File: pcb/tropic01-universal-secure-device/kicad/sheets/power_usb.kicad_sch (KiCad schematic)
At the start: 0 parts

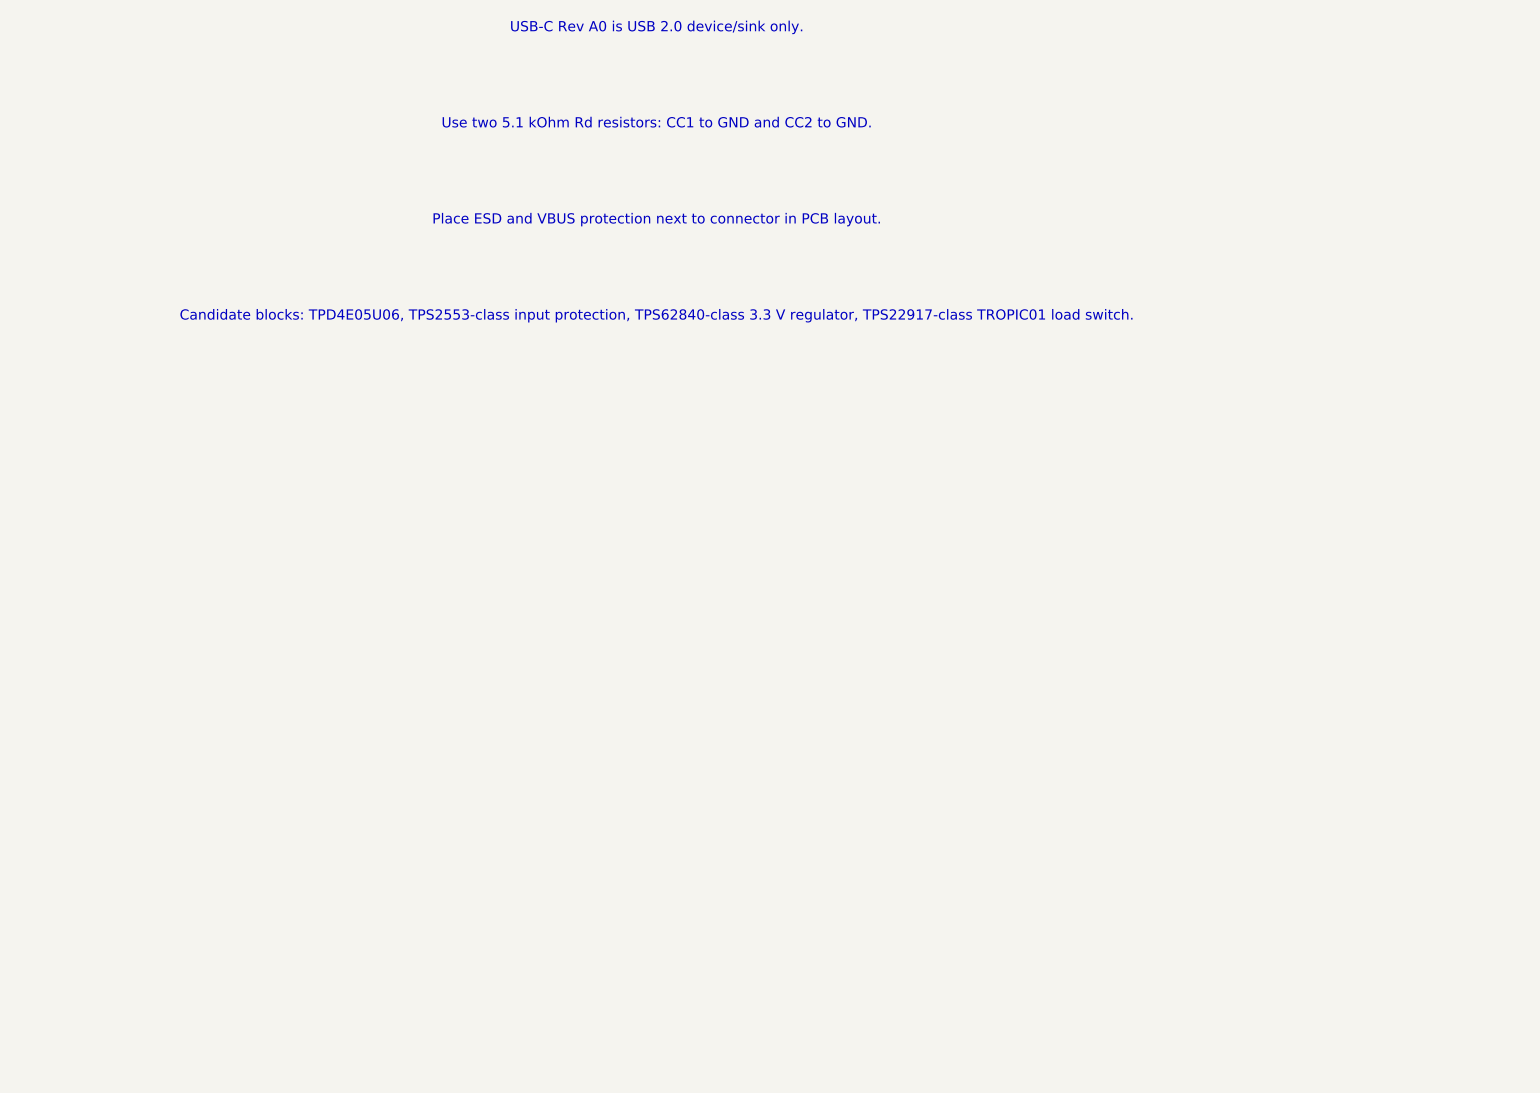
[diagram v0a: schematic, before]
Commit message: feat: materialize tropic01 schematic bindings
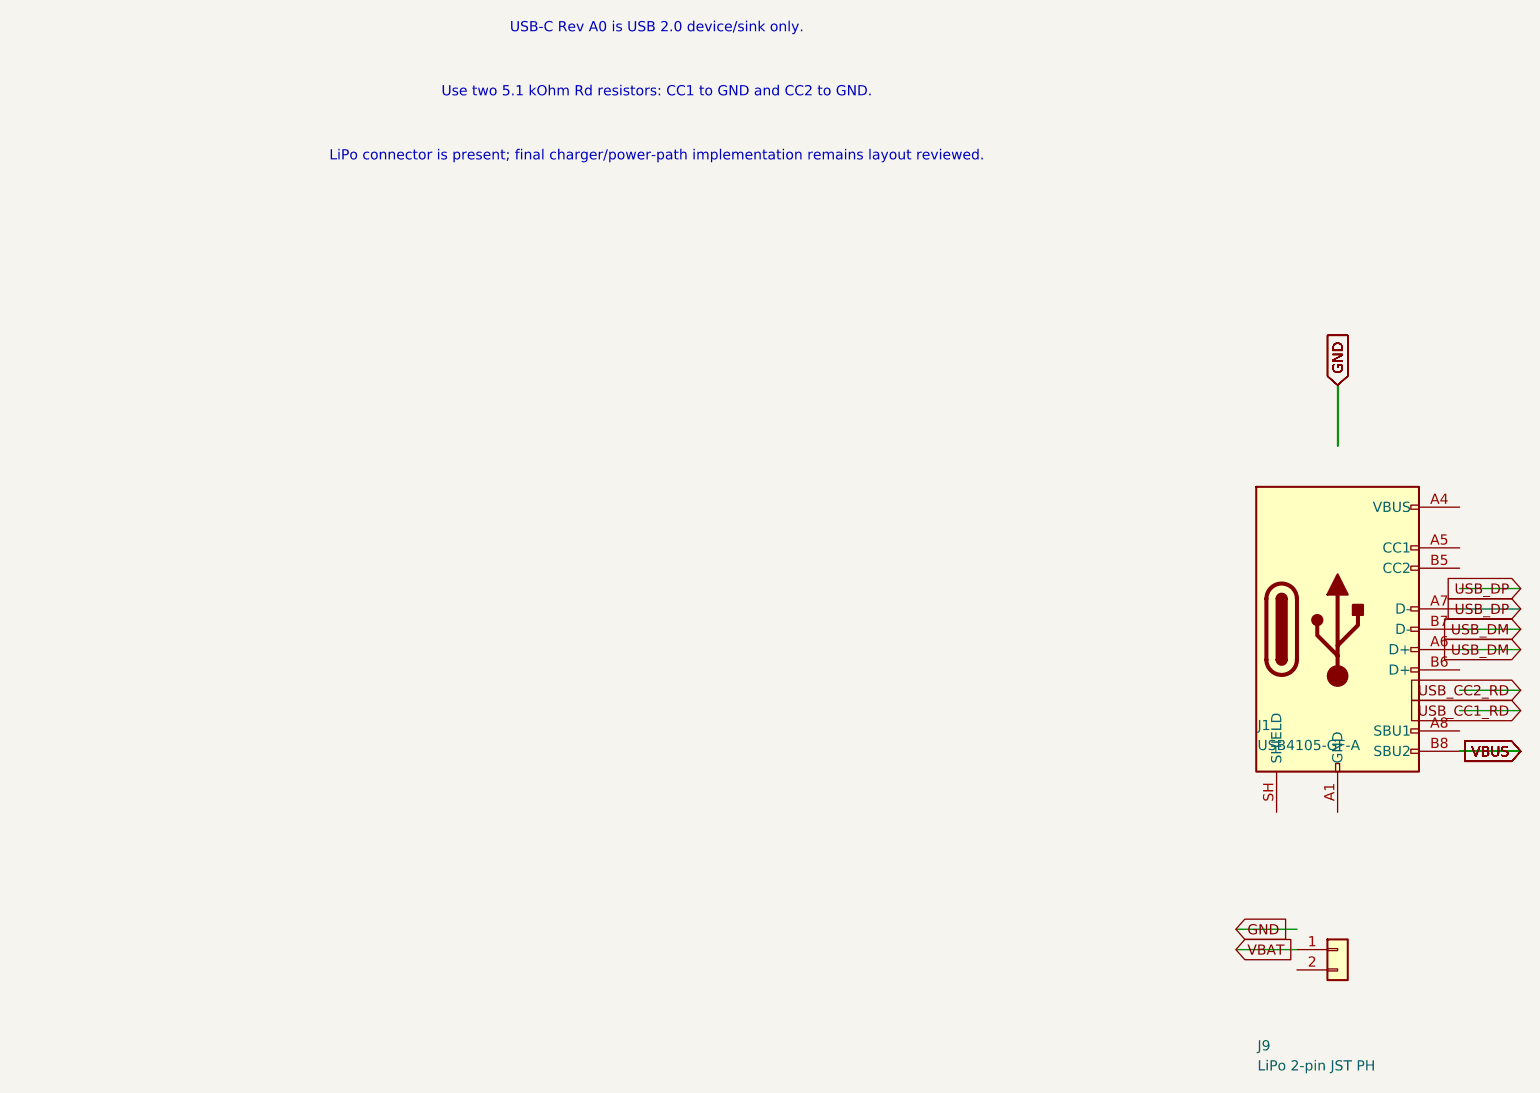
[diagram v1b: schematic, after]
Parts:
- added J1: USB4105-GF-A, Connector_USB:USB_C_Receptacle_GCT_USB4105-xx-A_16P_TopMnt_Horizontal, symbol Connector:USB_C_Receptacle_USB2.0_16P
- added J9: LiPo 2-pin JST PH, Connector_JST:JST_PH_S2B-PH-SM4-TB_1x02-1MP_P2.00mm_Horizontal, symbol Connector_Generic:Conn_01x02
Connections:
- new net: J1.A1 (GND), J1.A12 (GND), J1.B1 (GND), J1.B12 (GND)
- new net: J1.A4 (VBUS), J1.A9 (VBUS), J1.B4 (VBUS), J1.B9 (VBUS)
- new net USB_DM: J1.A6 (D+), J1.B7 (D-)
- new net USB_DP: J1.A7 (D-)
- new net VBAT: J9.1 (Pin_1)
- new net VBUS: J1.B8 (SBU2)
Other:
- note added: "LiPo connector is present; final charger/power-path implementation remains layout reviewed."
- note removed: "Candidate blocks: TPD4E05U06, TPS2553-class input protection, TPS62840-class 3.3 V regulator, TPS22917-class TROPIC01 load switch."
- note removed: "Place ESD and VBUS protection next to connector in PCB layout."

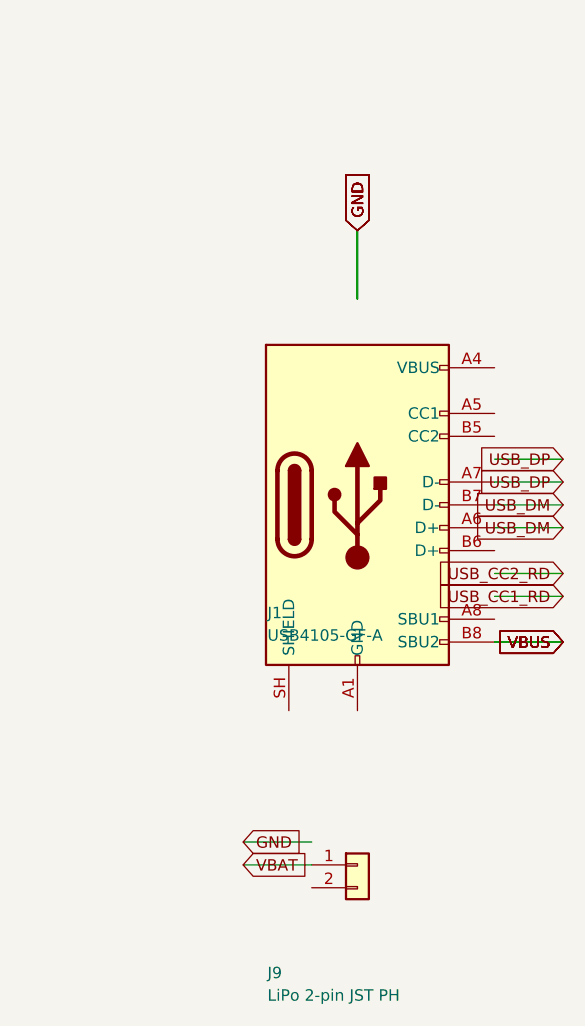
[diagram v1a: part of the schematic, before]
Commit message: feat: bind tropic01 pcb nets
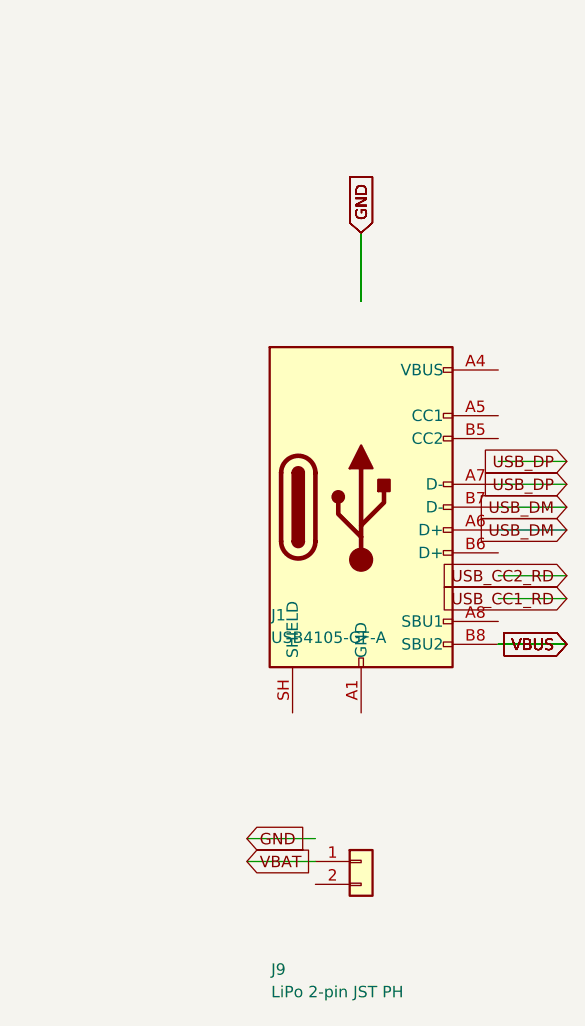
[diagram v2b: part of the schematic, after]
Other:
- moved on the sheet: J9
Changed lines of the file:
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@@
 	(symbol
 		(lib_id "Connector:USB_C_Receptacle_USB2.0_16P")
-		(at 105.00 95.00 0)
+		(at 105.41 95.25 0)
 		(unit 1)
 		(exclude_from_sim no)
@@
 		(dnp no)
 		(property "Reference" "J1"
-			(at 95.00 107.00 0)
+			(at 95.41 107.25 0)
 			(effects (font (size 1.27 1.27)) (justify left))
 		)
 		(property "Value" "USB4105-GF-A"
-			(at 95.00 109.50 0)
+			(at 95.41 109.75 0)
 			(effects (font (size 1.27 1.27)) (justify left))
 		)
 		(property "Footprint" "Connector_USB:USB_C_Receptacle_GCT_USB4105-xx-A_16P_TopMnt_Horizontal"
-			(at 105.00 95.00 0)
+			(at 105.41 95.25 0)
 			(effects (font (size 1.27 1.27)) (hide yes))
 		)
 		(property "Datasheet" "https://gct.co/connector/usb4105"
-			(at 105.00 95.00 0)
+			(at 105.41 95.25 0)
 			(effects (font (size 1.27 1.27)) (hide yes))
 		)
 		(property "Description" "GCT USB4105 USB 2.0 Type-C receptacle, female USB-C only"
-			(at 105.00 95.00 0)
+			(at 105.41 95.25 0)
 			(effects (font (size 1.27 1.27)) (hide yes))
 		)
@@
 	(symbol
 		(lib_id "Connector_Generic:Conn_01x02")
-		(at 105.00 135.00 0)
+		(at 105.41 134.62 0)
 		(unit 1)
 		(exclude_from_sim no)
@@
 		(dnp no)
 		(property "Reference" "J9"
-			(at 95.00 147.00 0)
+			(at 95.41 146.62 0)
 			(effects (font (size 1.27 1.27)) (justify left))
 		)
 		(property "Value" "LiPo 2-pin JST PH"
-			(at 95.00 149.50 0)
+			(at 95.41 149.12 0)
 			(effects (font (size 1.27 1.27)) (justify left))
 		)
 		(property "Footprint" "Connector_JST:JST_PH_S2B-PH-SM4-TB_1x02-1MP_P2.00mm_Horizontal"
-			(at 105.00 135.00 0)
+			(at 105.41 134.62 0)
 			(effects (font (size 1.27 1.27)) (hide yes))
 		)
 		(property "Datasheet" "https://www.jst.com/products/crimp-style-connectors-wire-to-board-type/ph-connector/"
-			(at 105.00 135.00 0)
+			(at 105.41 134.62 0)
 			(effects (font (size 1.27 1.27)) (hide yes))
 		)
 		(property "Description" "2-pin LiPo battery connector into charger/power path"
-			(at 105.00 135.00 0)
+			(at 105.41 134.62 0)
 			(effects (font (size 1.27 1.27)) (hide yes))
 		)
@@
 	(wire
 		(pts
-			(xy 105.00 72.14) (xy 105.00 64.52)
-		)
-		(stroke (width 0) (type default))
-	)
-	(global_label "GND"
-		(shape input)
-		(at 105.00 64.52 90)
-		(fields_autoplaced)
-		(effects (font (size 1.27 1.27)))
-	)
-	(wire
-		(pts
-			(xy 105.00 72.14) (xy 105.00 64.52)
-		)
-		(stroke (width 0) (type default))
-	)
-	(global_label "GND"
-		(shape input)
-		(at 105.00 64.52 90)
-		(fields_autoplaced)
-		(effects (font (size 1.27 1.27)))
-	)
-	(wire
-		(pts
-			(xy 120.24 110.24) (xy 127.86 110.24)
-		)
-		(stroke (width 0) (type default))
-	)
-	(global_label "VBUS"
-		(shape input)
-		(at 127.86 110.24 180)
-		(fields_autoplaced)
-		(effects (font (size 1.27 1.27)))
-	)
-	(wire
-		(pts
-			(xy 120.24 105.16) (xy 127.86 105.16)
+			(xy 105.41 72.39) (xy 105.41 64.77)
+		)
+		(stroke (width 0) (type default))
+	)
+	(global_label "GND"
+		(shape input)
+		(at 105.41 64.77 90)
+		(fields_autoplaced)
+		(effects (font (size 1.27 1.27)))
+	)
+	(wire
+		(pts
+			(xy 105.41 72.39) (xy 105.41 64.77)
+		)
+		(stroke (width 0) (type default))
+	)
+	(global_label "GND"
+		(shape input)
+		(at 105.41 64.77 90)
+		(fields_autoplaced)
+		(effects (font (size 1.27 1.27)))
+	)
+	(wire
+		(pts
+			(xy 120.65 110.49) (xy 128.27 110.49)
+		)
+		(stroke (width 0) (type default))
+	)
+	(global_label "VBUS"
+		(shape input)
+		(at 128.27 110.49 180)
+		(fields_autoplaced)
+		(effects (font (size 1.27 1.27)))
+	)
+	(wire
+		(pts
+			(xy 120.65 105.41) (xy 128.27 105.41)
 		)
 		(stroke (width 0) (type default))
@@
 	(global_label "USB_CC1_RD"
 		(shape input)
-		(at 127.86 105.16 180)
-		(fields_autoplaced)
-		(effects (font (size 1.27 1.27)))
-	)
-	(wire
-		(pts
-			(xy 120.24 92.46) (xy 127.86 92.46)
+		(at 128.27 105.41 180)
+		(fields_autoplaced)
+		(effects (font (size 1.27 1.27)))
+	)
+	(wire
+		(pts
+			(xy 120.65 92.71) (xy 128.27 92.71)
 		)
 		(stroke (width 0) (type default))
@@
 	(global_label "USB_DP"
 		(shape input)
-		(at 127.86 92.46 180)
-		(fields_autoplaced)
-		(effects (font (size 1.27 1.27)))
-	)
-	(wire
-		(pts
-			(xy 120.24 97.54) (xy 127.86 97.54)
+		(at 128.27 92.71 180)
+		(fields_autoplaced)
+		(effects (font (size 1.27 1.27)))
+	)
+	(wire
+		(pts
+			(xy 120.65 97.79) (xy 128.27 97.79)
 		)
 		(stroke (width 0) (type default))
@@
 	(global_label "USB_DM"
 		(shape input)
-		(at 127.86 97.54 180)
-		(fields_autoplaced)
-		(effects (font (size 1.27 1.27)))
-	)
-	(wire
-		(pts
-			(xy 120.24 110.24) (xy 127.86 110.24)
-		)
-		(stroke (width 0) (type default))
-	)
-	(global_label "VBUS"
-		(shape input)
-		(at 127.86 110.24 180)
-		(fields_autoplaced)
-		(effects (font (size 1.27 1.27)))
-	)
-	(wire
-		(pts
-			(xy 105.00 72.14) (xy 105.00 64.52)
-		)
-		(stroke (width 0) (type default))
-	)
-	(global_label "GND"
-		(shape input)
-		(at 105.00 64.52 90)
-		(fields_autoplaced)
-		(effects (font (size 1.27 1.27)))
-	)
-	(wire
-		(pts
-			(xy 105.00 72.14) (xy 105.00 64.52)
-		)
-		(stroke (width 0) (type default))
-	)
-	(global_label "GND"
-		(shape input)
-		(at 105.00 64.52 90)
-		(fields_autoplaced)
-		(effects (font (size 1.27 1.27)))
-	)
-	(wire
-		(pts
-			(xy 120.24 110.24) (xy 127.86 110.24)
-		)
-		(stroke (width 0) (type default))
-	)
-	(global_label "VBUS"
-		(shape input)
-		(at 127.86 110.24 180)
-		(fields_autoplaced)
-		(effects (font (size 1.27 1.27)))
-	)
-	(wire
-		(pts
-			(xy 120.24 102.62) (xy 127.86 102.62)
+		(at 128.27 97.79 180)
+		(fields_autoplaced)
+		(effects (font (size 1.27 1.27)))
+	)
+	(wire
+		(pts
+			(xy 120.65 110.49) (xy 128.27 110.49)
+		)
+		(stroke (width 0) (type default))
+	)
+	(global_label "VBUS"
+		(shape input)
+		(at 128.27 110.49 180)
+		(fields_autoplaced)
+		(effects (font (size 1.27 1.27)))
+	)
+	(wire
+		(pts
+			(xy 105.41 72.39) (xy 105.41 64.77)
+		)
+		(stroke (width 0) (type default))
+	)
+	(global_label "GND"
+		(shape input)
+		(at 105.41 64.77 90)
+		(fields_autoplaced)
+		(effects (font (size 1.27 1.27)))
+	)
+	(wire
+		(pts
+			(xy 105.41 72.39) (xy 105.41 64.77)
+		)
+		(stroke (width 0) (type default))
+	)
+	(global_label "GND"
+		(shape input)
+		(at 105.41 64.77 90)
+		(fields_autoplaced)
+		(effects (font (size 1.27 1.27)))
+	)
+	(wire
+		(pts
+			(xy 120.65 110.49) (xy 128.27 110.49)
+		)
+		(stroke (width 0) (type default))
+	)
+	(global_label "VBUS"
+		(shape input)
+		(at 128.27 110.49 180)
+		(fields_autoplaced)
+		(effects (font (size 1.27 1.27)))
+	)
+	(wire
+		(pts
+			(xy 120.65 102.87) (xy 128.27 102.87)
 		)
 		(stroke (width 0) (type default))
@@
 	(global_label "USB_CC2_RD"
 		(shape input)
-		(at 127.86 102.62 180)
-		(fields_autoplaced)
-		(effects (font (size 1.27 1.27)))
-	)
-	(wire
-		(pts
-			(xy 120.24 89.92) (xy 127.86 89.92)
+		(at 128.27 102.87 180)
+		(fields_autoplaced)
+		(effects (font (size 1.27 1.27)))
+	)
+	(wire
+		(pts
+			(xy 120.65 90.17) (xy 128.27 90.17)
 		)
 		(stroke (width 0) (type default))
@@
 	(global_label "USB_DP"
 		(shape input)
-		(at 127.86 89.92 180)
-		(fields_autoplaced)
-		(effects (font (size 1.27 1.27)))
-	)
-	(wire
-		(pts
-			(xy 120.24 95.00) (xy 127.86 95.00)
+		(at 128.27 90.17 180)
+		(fields_autoplaced)
+		(effects (font (size 1.27 1.27)))
+	)
+	(wire
+		(pts
+			(xy 120.65 95.25) (xy 128.27 95.25)
 		)
 		(stroke (width 0) (type default))
@@
 	(global_label "USB_DM"
 		(shape input)
-		(at 127.86 95.00 180)
-		(fields_autoplaced)
-		(effects (font (size 1.27 1.27)))
-	)
-	(wire
-		(pts
-			(xy 120.24 110.24) (xy 127.86 110.24)
-		)
-		(stroke (width 0) (type default))
-	)
-	(global_label "VBUS"
-		(shape input)
-		(at 127.86 110.24 180)
-		(fields_autoplaced)
-		(effects (font (size 1.27 1.27)))
-	)
-	(wire
-		(pts
-			(xy 99.92 135.00) (xy 92.30 135.00)
+		(at 128.27 95.25 180)
+		(fields_autoplaced)
+		(effects (font (size 1.27 1.27)))
+	)
+	(wire
+		(pts
+			(xy 120.65 110.49) (xy 128.27 110.49)
+		)
+		(stroke (width 0) (type default))
+	)
+	(global_label "VBUS"
+		(shape input)
+		(at 128.27 110.49 180)
+		(fields_autoplaced)
+		(effects (font (size 1.27 1.27)))
+	)
+	(wire
+		(pts
+			(xy 100.33 134.62) (xy 92.71 134.62)
 		)
 		(stroke (width 0) (type default))
@@
 	(global_label "VBAT"
 		(shape input)
-		(at 92.30 135.00 0)
-		(fields_autoplaced)
-		(effects (font (size 1.27 1.27)))
-	)
-	(wire
-		(pts
-			(xy 99.92 132.46) (xy 92.30 132.46)
-		)
-		(stroke (width 0) (type default))
-	)
-	(global_label "GND"
-		(shape input)
-		(at 92.30 132.46 0)
-		(fields_autoplaced)
-		(effects (font (size 1.27 1.27)))
+		(at 92.71 134.62 0)
+		(fields_autoplaced)
+		(effects (font (size 1.27 1.27)))
+	)
+	(wire
+		(pts
+			(xy 100.33 132.08) (xy 92.71 132.08)
+		)
+		(stroke (width 0) (type default))
+	)
+	(global_label "GND"
+		(shape input)
+		(at 92.71 132.08 0)
+		(fields_autoplaced)
+		(effects (font (size 1.27 1.27)))
